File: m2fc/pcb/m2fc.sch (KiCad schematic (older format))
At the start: 48 parts, among them IC101 ADP3335, IC102 STM32F405VGT, P101 CONN_2, P102 CONN_2, P103 SWD, U101 BAT BOX, U102 ARM SW, U103 MICROSD, U104 HOUSING, U105 HOUSING, X101 8M

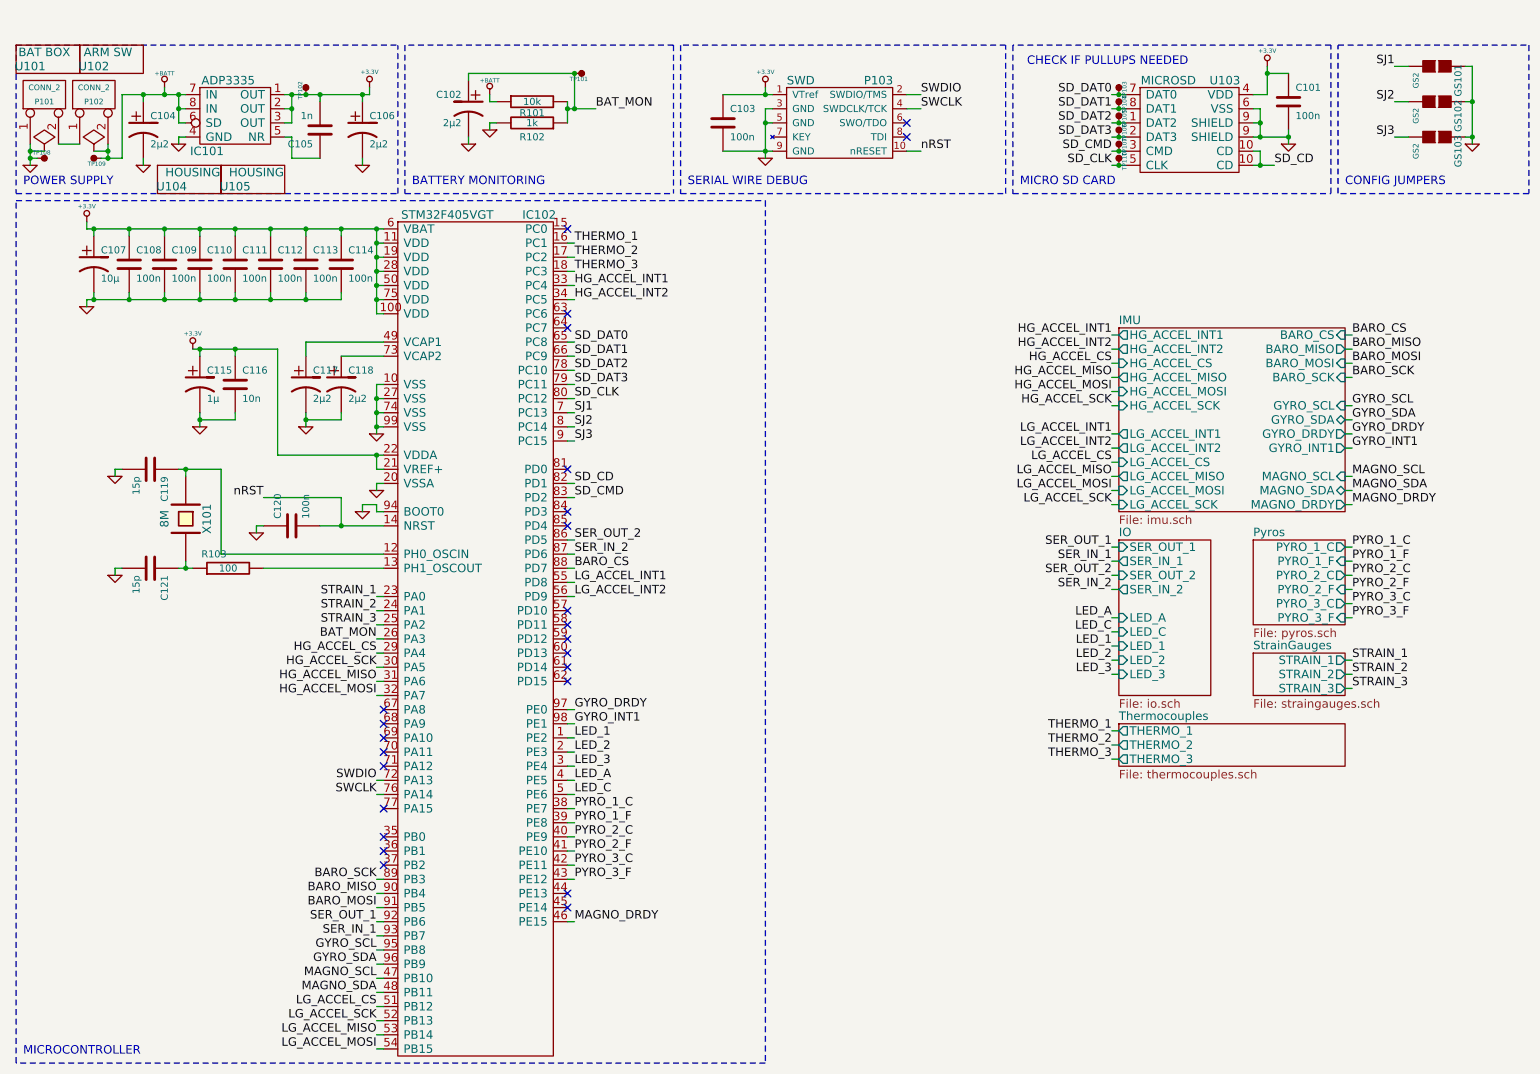
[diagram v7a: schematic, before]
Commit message: sd pullups, shielded sgs
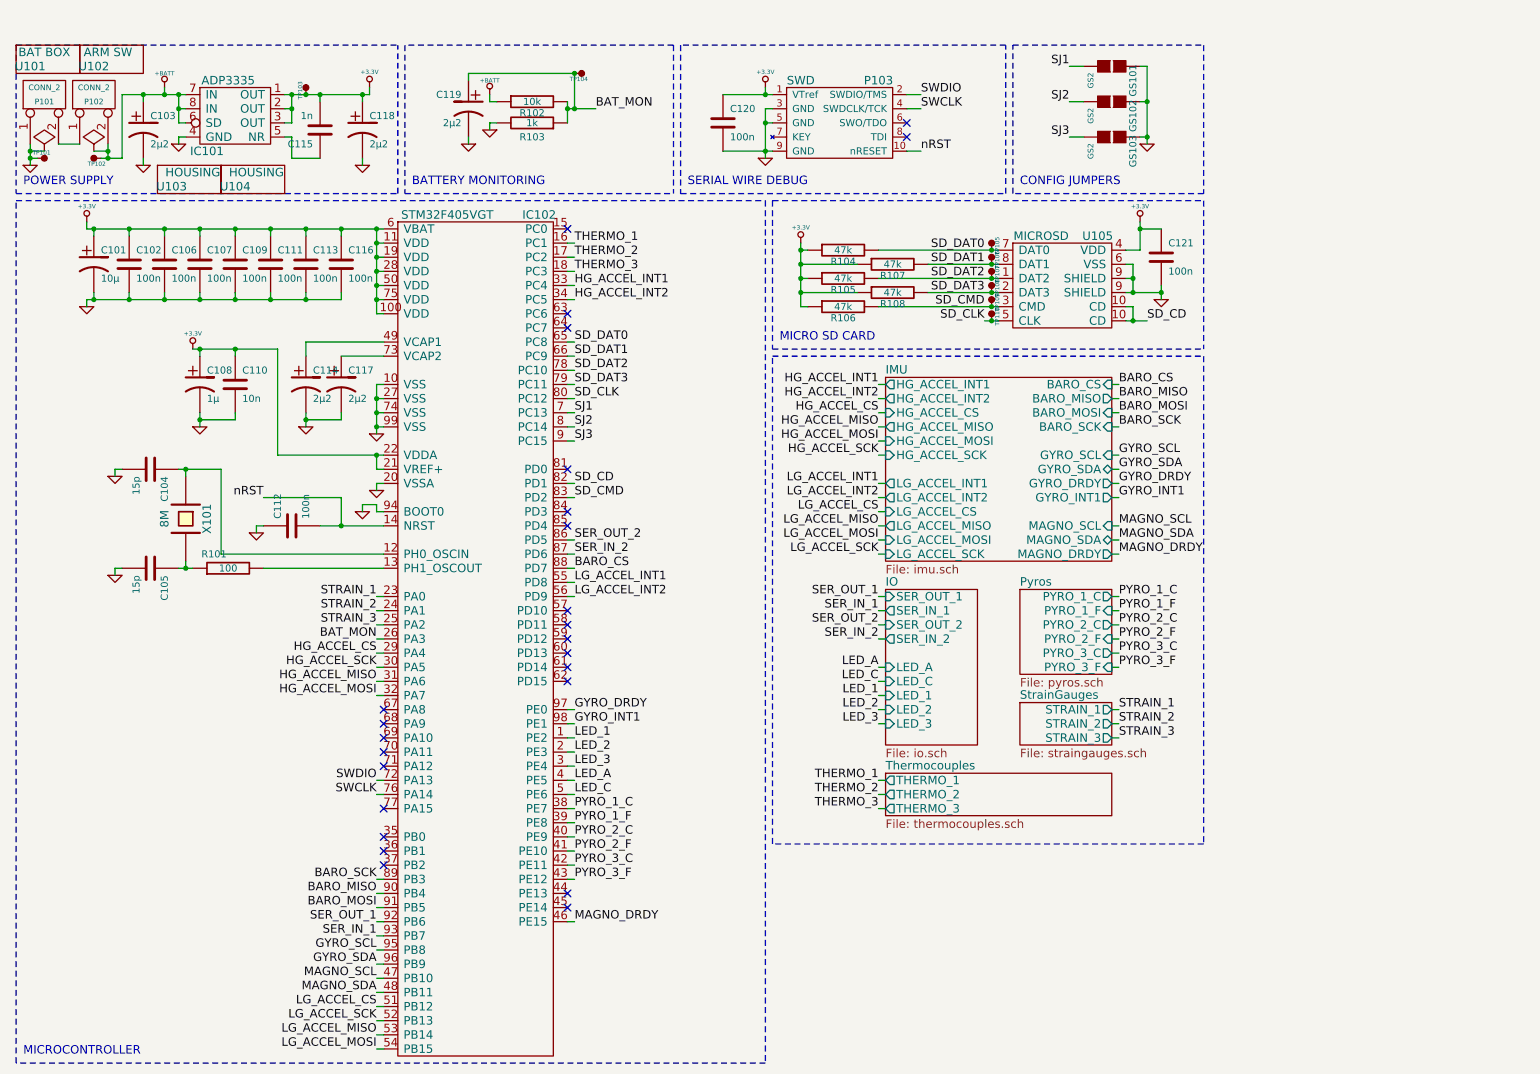
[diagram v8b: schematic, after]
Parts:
- added R104, R105, R106, R107, R108: 47k, m2fc:R0603, symbol R
- C102: renamed from C108; footprint 0603 -> m2fc:C0603
- C103: renamed from C104; footprint 0603 -> m2fc:C0603
- C104: renamed from C119; footprint 0603 -> m2fc:C0603
- C105: renamed from C121; footprint 0603 -> m2fc:C0603
- C106: renamed from C109; footprint 0603 -> m2fc:C0603
- C107: renamed from C110; footprint 0603 -> m2fc:C0603
- C109: renamed from C111; footprint 0603 -> m2fc:C0603
- C110: renamed from C116; footprint 0603 -> m2fc:C0603
- C111: renamed from C112; footprint 0603 -> m2fc:C0603
- C112: renamed from C120; footprint 0603 -> m2fc:C0603
- C113: footprint 0603 -> m2fc:C0603
- C114: renamed from C117; footprint 0603 -> m2fc:C0603
- C115: renamed from C105; footprint 0603 -> m2fc:C0603
- C116: renamed from C114; footprint 0603 -> m2fc:C0603
- C117: renamed from C118; footprint 0603 -> m2fc:C0603
- C118: renamed from C106; footprint 0603 -> m2fc:C0603
- C119: renamed from C102; footprint 0603 -> m2fc:C0603
- C120: renamed from C103; footprint 0603 -> m2fc:C0603
- C121: renamed from C101; footprint 0603 -> m2fc:C0603
- GS101, GS102, GS103: footprint GS2 -> Connect:GS2
- IC101: footprint MSOP-8 -> m2fc:MSOP8
- P101, P102: footprint (none) -> m2fc:S02B-PASK-2
- P103: footprint (none) -> m2fc:FTSH-105-01-F-D-K
- R101: renamed from R103; footprint 0603 -> m2fc:R0603
- R102: renamed from R101; footprint 0603 -> m2fc:R0603
- R103: renamed from R102; footprint 0603 -> m2fc:R0603
- TP101: renamed from TP108; footprint (none) -> m2fc:TESTPAD
- TP102: renamed from TP109; footprint (none) -> m2fc:TESTPAD
- TP103: renamed from TP102; footprint (none) -> m2fc:TESTPAD
- TP104: renamed from TP101; footprint (none) -> m2fc:TESTPAD
- TP105: renamed from TP103; footprint (none) -> m2fc:TESTPAD
- TP106: renamed from TP104; footprint (none) -> m2fc:TESTPAD
- TP107: renamed from TP105; footprint (none) -> m2fc:TESTPAD
- TP108: renamed from TP106; footprint (none) -> m2fc:TESTPAD
- TP109: renamed from TP107; footprint (none) -> m2fc:TESTPAD
- TP110: footprint (none) -> m2fc:TESTPAD
- X101: footprint HC49/S -> m2fc:HC49S
- renumbered C107 to C101, C115 to C108, U104 to U103, U105 to U104, U103 to U105
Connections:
- net +3.3V: now also R104.1, R105.1, R106.1, R107.1, R108.1
- net SD_CMD: now also R106.2
- net SD_DAT0: now also R104.2
- net SD_DAT1: now also R107.2
- net SD_DAT2: now also R105.2
- net SD_DAT3: now also R108.2
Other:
- note removed: "CHECK IF PULLUPS NEEDED"
- moved on the sheet: C121, GS101, GS102, GS103, TP105, TP106, TP107, TP108, TP109, TP110, U105
